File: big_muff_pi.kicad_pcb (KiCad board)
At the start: 2 copper layers, 80 x 100 mm, 67 parts, among them J1 NMJ6HHD2, J2 NMJ6HHD2, J3 Conn_01x05, J4 Conn_01x05, J5 Conn_01x05, J6 Barrel_Jack_MountingPin, Q1 MMBT5551, Q2 MMBT5551, Q3 MMBT5551, Q4 MMBT5551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

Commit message: Estetics finalized.
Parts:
- added D8: floating_green_led, pedale:floating_green_led, F.Cu at (74.0, 117.0)
- added D9: floating_red_led, pedale:floating_red_led, F.Cu at (106.0, 117.0)
- added H5: MountingHole, pedale:M3_hole_with_spacer, F.Cu at (90.0, 145.0)
- added REF**: big_muff_pi_front_plate, pedale:big_muff_pi_front_plate, F.Cu at (90.0, 95.0)
- added RV1: floating_pot_knob, pedale:floating_pot_knob, F.Cu at (68.0, 69.0)
- added RV2: floating_pot_knob, pedale:floating_pot_knob, F.Cu at (90.0, 69.0)
- added RV3: floating_pot_knob, pedale:floating_pot_knob, F.Cu at (112.0, 69.0)
- added RV4: floating_pot, pedale:floating_pot, F.Cu at (68.0, 69.0)
- added RV5: floating_pot, pedale:floating_pot, F.Cu at (90.0, 69.0)
- added RV6: floating_pot, pedale:floating_pot, F.Cu at (112.0, 69.0)
- moved R23 81.4 mm to (56.9, 105.5)
- moved D6 74.0 mm to (59.5, 109.5)
- moved C19 7.18 mm to (60.5, 68.0)
- moved SW1 1.41 mm to (85.0, 122.5)
- moved J2 1.10 mm to (67.2, 133.1)
- moved J1 1.10 mm to (112.8, 116.9)
- moved BT1 0.65 mm to (70.8, 89.7)

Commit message: Est
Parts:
- removed D6: LED, LED_THT:LED_D5.0mm
- removed R23: 1k, Resistor_SMD:R_0603_1608Metric_Pad0.98x0.95mm_HandSolder
- removed REF**: big_muff_pi_front_plate, pedale:big_muff_pi_front_plate
- added P1: big_muff_pi_front_panel, pedale:big_muff_pi_front_plate, F.Cu at (50.0, 50.0)
- added R25: 1k, Resistor_SMD:R_0603_1608Metric_Pad0.98x0.95mm_HandSolder, F.Cu at (61.0, 108.0)
- added R26: 1k, Resistor_SMD:R_0603_1608Metric_Pad0.98x0.95mm_HandSolder, F.Cu at (61.0, 110.5)
- added SIM1: Logo_Open_Hardware_Small, Symbol:OSHW-Logo2_7.3x6mm_SilkScreen, F.Cu at (107.5, 145.0)
- moved D7 70.9 mm to (122.1, 59.6), turned to 180 degrees
- moved C20 66.2 mm to (121.1, 65.9), turned to 180 degrees
- moved C19 55.5 mm to (115.9, 71.9), turned to -90 degrees
- moved R3 48.8 mm to (64.5, 64.1), turned to -90 degrees
- moved C2 46.3 mm to (65.3, 66.7), turned to 0 degrees
- moved R1 45.7 mm to (66.1, 64.1), turned to 90 degrees
- moved R6 43.8 mm to (66.8, 74.6), turned to 90 degrees
- moved J3 43.0 mm to (63.0, 55.0)
- moved J5 43.0 mm to (106.0, 55.0)
- moved R7 39.0 mm to (69.5, 75.4), turned to 0 degrees
- moved R2 38.9 mm to (68.8, 71.1), turned to 90 degrees
- moved R10 38.1 mm to (69.5, 73.7), turned to 0 degrees
- moved R4 38.1 mm to (70.3, 63.4), turned to 0 degrees
- moved C1 37.1 mm to (70.3, 65.0), turned to 0 degrees
- moved Q4 36.3 mm to (70.2, 67.6), turned to 0 degrees
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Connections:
- J3 pad 1: 0 -> 9V
- J3 pad 2: FS_OUT -> Net-(J3-Pin_2)
- J3 pad 4: Net-(J3-Pin_4) -> FS_OUT
- J3 pad 5: 0 -> Net-(J3-Pin_5)
- J5 pad 1: 0 -> Net-(J5-Pin_1)
- J5 pad 5: 0 -> Net-(J5-Pin_5)
- R6 pad 1: Net-(J3-Pin_4) -> Net-(J3-Pin_2)
- SW1 pad 5: Net-(D6-A) -> Net-(J5-Pin_5)
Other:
- board text added: "BIG MUFF PI"

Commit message: Only routing left.
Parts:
- moved R26 75.8 mm to (117.2, 59.7), turned to -90 degrees
- moved C20 67.4 mm to (59.0, 92.1), turned to -90 degrees
- moved D7 67.0 mm to (64.8, 94.4), turned to -90 degrees
- moved C19 59.4 mm to (57.0, 80.0), turned to 90 degrees
- moved R25 55.1 mm to (77.0, 55.3), turned to -90 degrees
- moved R24 48.0 mm to (57.1, 87.7), turned to 90 degrees
- moved C14 44.0 mm to (62.3, 87.0)
- moved Q5 42.3 mm to (60.5, 84.4), turned to 180 degrees
- moved C18 42.1 mm to (62.3, 88.5), turned to 180 degrees
- moved D4 41.0 mm to (64.8, 83.6)
- moved C16 37.5 mm to (63.2, 81.1)
- moved C17 35.5 mm to (63.2, 79.4), turned to 0 degrees
- moved J6 6.30 mm to (63.9, 103.3)
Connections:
- C11 pad 2: Net-(J5-Pin_4) -> Net-(J5-Pin_3)
- C12 pad 2: Net-(J4-Pin_4) -> Net-(J4-Pin_3)
- C13 pad 2: Net-(J4-Pin_2) -> Net-(J4-Pin_1)
- J1 pad S: unconnected-(J1-PadS) -> 0
- J2 pad S: unconnected-(J2-PadS) -> 0
- J3 pad 1: 9V -> Net-(J3-Pin_1)
- J3 pad 3: Net-(J3-Pin_3) -> FS_OUT
- J3 pad 4: FS_OUT -> 9V
- J4 pad 1: 0 -> Net-(J4-Pin_1)
- J4 pad 2: Net-(J4-Pin_2) -> F_OUT
- J4 pad 3: F_OUT -> Net-(J4-Pin_3)
- J4 pad 4: Net-(J4-Pin_4) -> 0
- J5 pad 1: Net-(J5-Pin_1) -> 0
- J5 pad 2: 0 -> Net-(J5-Pin_2)
- R17 pad 2: Net-(J4-Pin_2) -> Net-(J4-Pin_1)
- R22 pad 2: Net-(J4-Pin_4) -> Net-(J4-Pin_3)
- R26 pad 1: Net-(J5-Pin_1) -> Net-(J5-Pin_5)
- R6 pad 1: Net-(J3-Pin_2) -> Net-(J3-Pin_1)
- R7 pad 1: Net-(J3-Pin_3) -> Net-(J3-Pin_2)
- SW1 pad 1: Net-(J5-Pin_3) -> Net-(J5-Pin_2)
- SW1 pad 5: Net-(J5-Pin_5) -> Net-(J5-Pin_4)

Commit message: Lib sync.
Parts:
- SW1: value SW_DPDT_x2 -> pedala_switch; footprint switch:switch_DPDT -> pedale:switch_DPDT
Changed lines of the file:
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@@
 	)
 	(footprint "pedale:floating_red_led"
+		(locked yes)
 		(layer "F.Cu")
 		(at 106 117)
@@
 		)
 	)
-	(footprint "switch:switch_DPDT"
-		(locked yes)
-		(layer "F.Cu")
-		(at 85 122.5)
-		(descr "C&K sub miniature slide switch, JS series, DPDT, right angle, http://www.ckswitches.com/media/1422/js.pdf")
-		(tags "switch DPDT")
-		(property "Reference" "SW1"
-			(at 5 -7 0)
-			(layer "F.SilkS")
-			(hide yes)
-			(effects
-				(font
-					(size 1 1)
-					(thickness 0.15)
-				)
-			)
-		)
-		(property "Value" "SW_DPDT_x2"
-			(at 5 9 0)
-			(layer "F.Fab")
-			(effects
-				(font
-					(size 1 1)
-					(thickness 0.15)
-				)
-			)
-		)
-		(property "Datasheet" ""
-			(at 0 0 0)
-			(unlocked yes)
-			(layer "F.Fab")
-			(hide yes)
-			(effects
-				(font
-					(size 1.27 1.27)
-					(thickness 0.15)
-				)
-			)
-		)
-		(property "Description" "Switch, dual pole double throw, separate symbols"
-			(at 0 0 0)
-			(unlocked yes)
-			(layer "F.Fab")
-			(hide yes)
-			(effects
-				(font
-					(size 1.27 1.27)
-					(thickness 0.15)
-				)
-			)
-		)
-		(property ki_fp_filters "SW*DPDT*")
-		(sheetname "/")
-		(sheetfile "big_muff_pi.kicad_sch")
-		(attr through_hole)
-		(fp_rect
-			(start -5.5 -6)
-			(end 15.5 11)
-			(stroke
-				(width 0.05)
-				(type default)
-			)
-			(fill no)
-			(layer "F.CrtYd")
-		)
-		(fp_text user "${REFERENCE}"
-			(at 6 -7 0)
-			(layer "F.Fab")
-			(effects
-				(font
-					(size 1 1)
-					(thickness 0.15)
-				)
-			)
-		)
-		(pad "1" thru_hole roundrect
-			(at 0 0)
-			(size 3.5 4.5)
-			(drill oval 2.5 3)
-			(layers "*.Cu" "*.Mask")
-			(remove_unused_layers no)
-			(roundrect_rratio 0.2857142857)
-			(net 34 "Net-(J5-Pin_2)")
-			(pinfunction "A")
-			(pintype "passive")
-			(thermal_bridge_angle 45)
-		)
-		(pad "2" thru_hole roundrect
-			(at 5 0)
-			(size 3.5 4.5)
-			(drill oval 2.5 3)
-			(layers "*.Cu" "*.Mask")
-			(remove_unused_layers no)
-			(roundrect_rratio 0.2857142857)
-			(net 35 "Net-(SW1A-B)")
-			(pinfunction "B")
-			(pintype "passive")
-			(thermal_bridge_angle 45)
-		)
-		(pad "3" thru_hole roundrect
-			(at 10 0)
-			(size 3.5 4.5)
-			(drill oval 2.5 3)
-			(layers "*.Cu" "*.Mask")
-			(remove_unused_layers no)
-			(roundrect_rratio 0.2857142857)
-			(net 37 "SW_IN")
-			(pinfunction "C")
-			(pintype "passive")
-			(thermal_bridge_angle 45)
-		)
-		(pad "4" thru_hole roundrect
-			(at 10 5)
-			(size 3.5 4.5)
-			(drill oval 2.5 3)
-			(layers "*.Cu" "*.Mask")
-			(remove_unused_layers no)
-			(roundrect_rratio 0.2857142857)
-			(net 14 "9V")
-			(pinfunction "A")
-			(pintype "passive")
-			(thermal_bridge_angle 45)
-		)
-		(pad "5" thru_hole roundrect
-			(at 5 5)
-			(size 3.5 4.5)
-			(drill oval 2.5 3)
-			(layers "*.Cu" "*.Mask")
-			(remove_unused_layers no)
-			(roundrect_rratio 0.2857142857)
-			(net 32 "Net-(J5-Pin_4)")
-			(pinfunction "B")
-			(pintype "passive")
-			(thermal_bridge_angle 45)
-		)
-		(pad "6" thru_hole roundrect
-			(at 0 5)
-			(size 3.5 4.5)
-			(drill oval 2.5 3)
-			(layers "*.Cu" "*.Mask")
-			(remove_unused_layers no)
-			(roundrect_rratio 0.2857142857)
-			(net 38 "unconnected-(SW1B-C-Pad6)")
-			(pinfunction "C")
-			(pintype "passive+no_connect")
-			(thermal_bridge_angle 45)
-		)
-		(embedded_fonts no)
-		(model "${KIPRJMOD}/switch.STEP"
-			(offset
-				(xyz 5 -2.5 12)
-			)
-			(scale
-				(xyz 1 1 1)
-			)
-			(rotate
-				(xyz -90 -0 -0)
-			)
-		)
-	)
 	(footprint "Diode_SMD:D_SOD-323"
 		(layer "F.Cu")
@@
 		)
 	)
+	(footprint "pedale:switch_DPDT"
+		(locked yes)
+		(layer "F.Cu")
+		(at 85 122.5)
+		(descr "C&K sub miniature slide switch, JS series, DPDT, right angle, http://www.ckswitches.com/media/1422/js.pdf")
+		(tags "switch DPDT")
+		(property "Reference" "SW1"
+			(at 5 -7 0)
+			(layer "F.SilkS")
+			(hide yes)
+			(effects
+				(font
+					(size 1 1)
+					(thickness 0.15)
+				)
+			)
+		)
+		(property "Value" "pedala_switch"
+			(at 5 9 0)
+			(layer "F.Fab")
+			(effects
+				(font
+					(size 1 1)
+					(thickness 0.15)
+				)
+			)
+		)
+		(property "Datasheet" ""
+			(at 0 0 0)
+			(unlocked yes)
+			(layer "F.Fab")
+			(hide yes)
+			(effects
+				(font
+					(size 1.27 1.27)
+					(thickness 0.15)
+				)
+			)
+		)
+		(property "Description" "Switch, dual pole double throw, separate symbols"
+			(at 0 0 0)
+			(unlocked yes)
+			(layer "F.Fab")
+			(hide yes)
+			(effects
+				(font
+					(size 1.27 1.27)
+					(thickness 0.15)
+				)
+			)
+		)
+		(property ki_fp_filters "SW*DPDT*")
+		(sheetname "/")
+		(sheetfile "big_muff_pi.kicad_sch")
+		(attr through_hole)
+		(fp_rect
+			(start -5.5 -6)
+			(end 15.5 11)
+			(stroke
+				(width 0.05)
+				(type default)
+			)
+			(fill no)
+			(layer "F.CrtYd")
+		)
+		(fp_text user "${REFERENCE}"
+			(at 6 -7 0)
+			(layer "F.Fab")
+			(effects
+				(font
+					(size 1 1)
+					(thickness 0.15)
+				)
+			)
+		)
+		(pad "1" thru_hole roundrect
+			(at 0 0)
+			(size 3.5 4.5)
+			(drill oval 2.5 3)
+			(layers "*.Cu" "*.Mask")
+			(remove_unused_layers no)
+			(roundrect_rratio 0.2857142857)
+			(net 34 "Net-(J5-Pin_2)")
+			(pinfunction "A")
+			(pintype "passive")
+			(thermal_bridge_angle 45)
+		)
+		(pad "2" thru_hole roundrect
+			(at 5 0)
+			(size 3.5 4.5)
+			(drill oval 2.5 3)
+			(layers "*.Cu" "*.Mask")
+			(remove_unused_layers no)
+			(roundrect_rratio 0.2857142857)
+			(net 35 "Net-(SW1A-B)")
+			(pinfunction "B")
+			(pintype "passive")
+			(thermal_bridge_angle 45)
+		)
+		(pad "3" thru_hole roundrect
+			(at 10 0)
+			(size 3.5 4.5)
+			(drill oval 2.5 3)
+			(layers "*.Cu" "*.Mask")
+			(remove_unused_layers no)
+			(roundrect_rratio 0.2857142857)
+			(net 37 "SW_IN")
+			(pinfunction "C")
+			(pintype "passive")
+			(thermal_bridge_angle 45)
+		)
+		(pad "4" thru_hole roundrect
+			(at 10 5)
+			(size 3.5 4.5)
+			(drill oval 2.5 3)
+			(layers "*.Cu" "*.Mask")
+			(remove_unused_layers no)
+			(roundrect_rratio 0.2857142857)
+			(net 14 "9V")
+			(pinfunction "A")
+			(pintype "passive")
+			(thermal_bridge_angle 45)
+		)
+		(pad "5" thru_hole roundrect
+			(at 5 5)
+			(size 3.5 4.5)
+			(drill oval 2.5 3)
+			(layers "*.Cu" "*.Mask")
+			(remove_unused_layers no)
+			(roundrect_rratio 0.2857142857)
+			(net 32 "Net-(J5-Pin_4)")
+			(pinfunction "B")
+			(pintype "passive")
+			(thermal_bridge_angle 45)
+		)
+		(pad "6" thru_hole roundrect
+			(at 0 5)
+			(size 3.5 4.5)
+			(drill oval 2.5 3)
+			(layers "*.Cu" "*.Mask")
+			(remove_unused_layers no)
+			(roundrect_rratio 0.2857142857)
+			(net 38 "unconnected-(SW1B-C-Pad6)")
+			(pinfunction "C")
+			(pintype "passive+no_connect")
+			(thermal_bridge_angle 45)
+		)
+		(embedded_fonts no)
+		(model "${KIPRJMOD}/switch.STEP"
+			(offset
+				(xyz 5 -2.5 12)
+			)
+			(scale
+				(xyz 1 1 1)
+			)
+			(rotate
+				(xyz -90 -0 -0)
+			)
+		)
+	)
 	(footprint "Package_TO_SOT_SMD:SOT-23"
 		(layer "F.Cu")
@@
 	)
 	(footprint "pedale:floating_green_led"
+		(locked yes)
 		(layer "F.Cu")
 		(at 74 117)
@@
 			(unlocked yes)
 			(layer "F.SilkS")
+			(hide yes)
 			(effects
 				(font

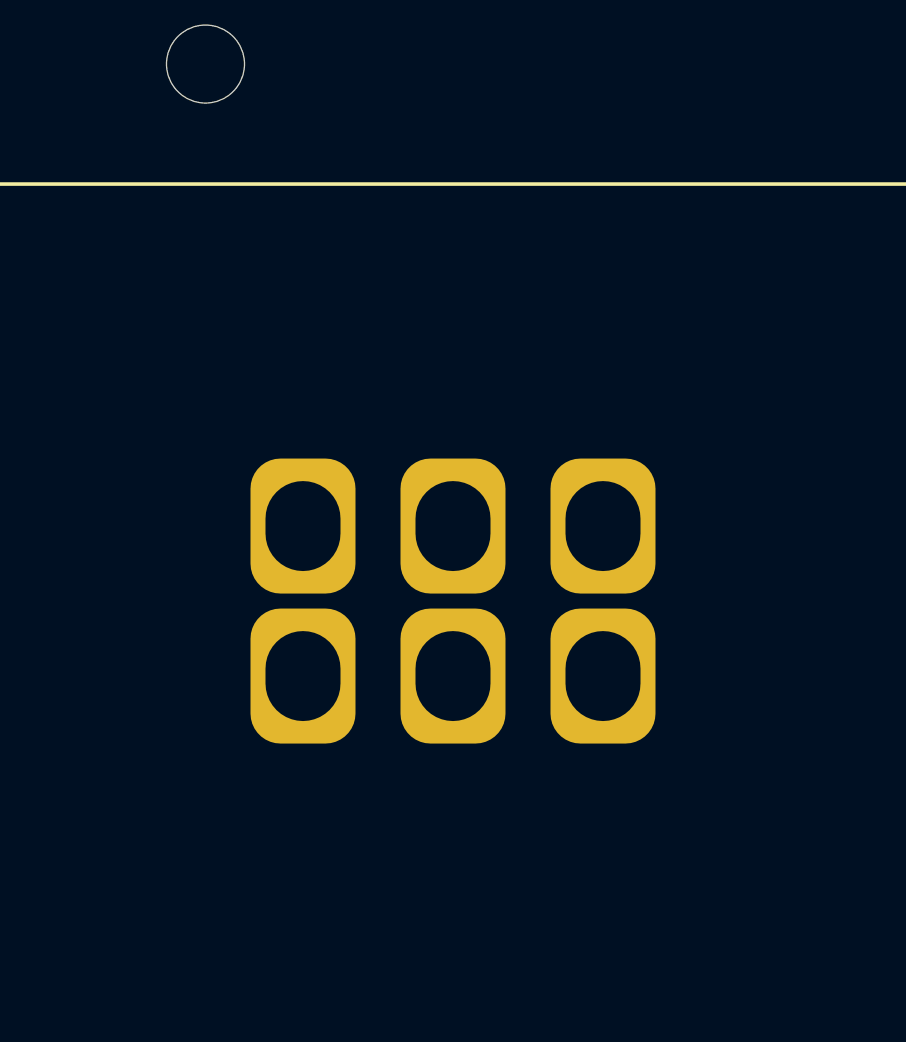
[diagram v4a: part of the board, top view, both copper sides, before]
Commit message: New switch
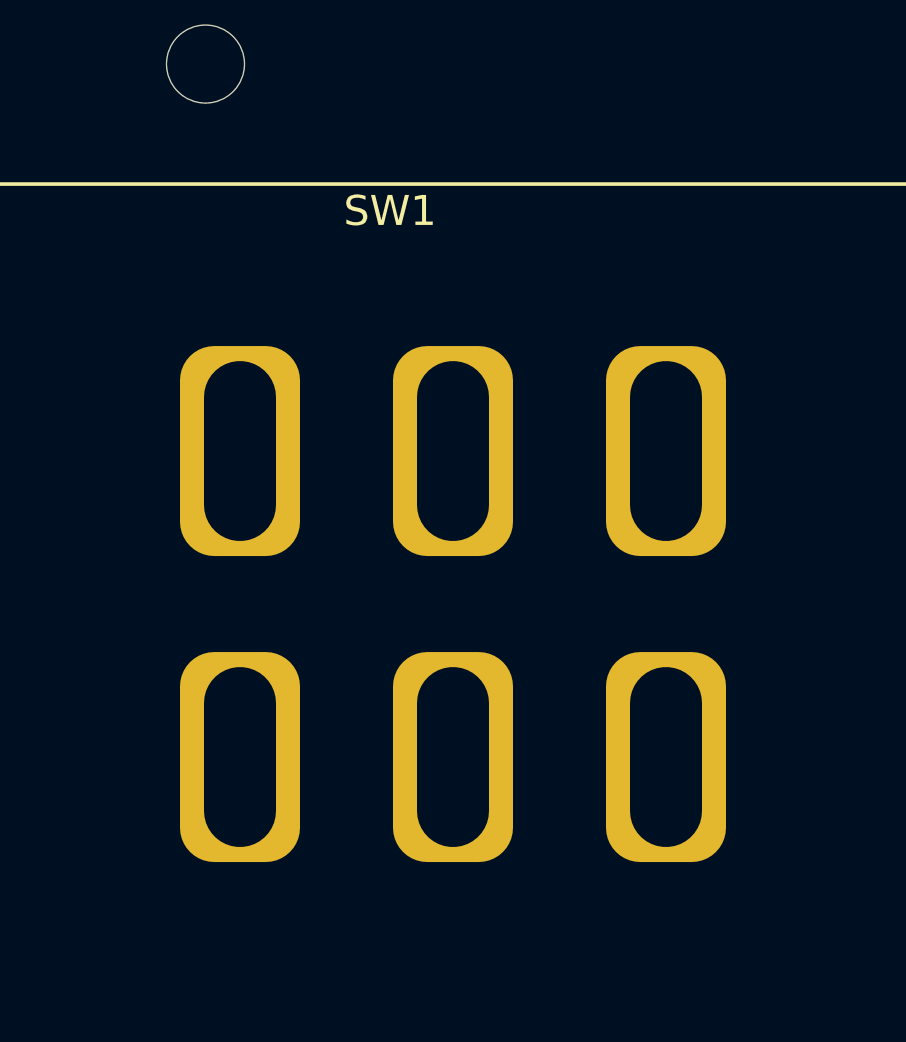
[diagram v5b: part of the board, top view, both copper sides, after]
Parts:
- SW1: footprint pedale:switch_DPDT -> pedale:foot_switch
- moved SW1 4.08 mm to (82.9, 119.0)
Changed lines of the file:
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@@
 		)
 	)
+	(footprint "pedale:foot_switch"
+		(layer "F.Cu")
+		(at 82.9 119)
+		(descr "C&K sub miniature slide switch, JS series, DPDT, right angle, http://www.ckswitches.com/media/1422/js.pdf")
+		(tags "switch DPDT")
+		(property "Reference" "SW1"
+			(at 5 -7 0)
+			(layer "F.SilkS")
+			(effects
+				(font
+					(size 1 1)
+					(thickness 0.15)
+				)
+			)
+		)
+		(property "Value" "pedala_switch"
+			(at 5 9 0)
+			(layer "F.Fab")
+			(effects
+				(font
+					(size 1 1)
+					(thickness 0.15)
+				)
+			)
+		)
+		(property "Datasheet" ""
+			(at 0 0 0)
+			(unlocked yes)
+			(layer "F.Fab")
+			(hide yes)
+			(effects
+				(font
+					(size 1.27 1.27)
+					(thickness 0.15)
+				)
+			)
+		)
+		(property "Description" "Switch, dual pole double throw, separate symbols"
+			(at 0 0 0)
+			(unlocked yes)
+			(layer "F.Fab")
+			(hide yes)
+			(effects
+				(font
+					(size 1.27 1.27)
+					(thickness 0.15)
+				)
+			)
+		)
+		(property ki_fp_filters "SW*DPDT*")
+		(sheetname "/")
+		(sheetfile "big_muff_pi.kicad_sch")
+		(attr through_hole)
+		(fp_rect
+			(start -3.5 -3)
+			(end 18 15)
+			(stroke
+				(width 0.05)
+				(type default)
+			)
+			(fill no)
+			(layer "F.CrtYd")
+		)
+		(fp_text user "${REFERENCE}"
+			(at 6 -7 0)
+			(layer "F.Fab")
+			(effects
+				(font
+					(size 1 1)
+					(thickness 0.15)
+				)
+			)
+		)
+		(pad "1" thru_hole roundrect
+			(at 0 1)
+			(size 4 7)
+			(drill oval 2.4 6)
+			(layers "*.Cu" "*.Mask")
+			(remove_unused_layers no)
+			(roundrect_rratio 0.2857142857)
+			(net 34 "Net-(J5-Pin_2)")
+			(pinfunction "A")
+			(pintype "passive")
+			(thermal_bridge_angle 45)
+		)
+		(pad "2" thru_hole roundrect
+			(at 7.1 1)
+			(size 4 7)
+			(drill oval 2.4 6)
+			(layers "*.Cu" "*.Mask")
+			(remove_unused_layers no)
+			(roundrect_rratio 0.2857142857)
+			(net 35 "Net-(SW1A-B)")
+			(pinfunction "B")
+			(pintype "passive")
+			(thermal_bridge_angle 45)
+		)
+		(pad "3" thru_hole roundrect
+			(at 14.2 1)
+			(size 4 7)
+			(drill oval 2.4 6)
+			(layers "*.Cu" "*.Mask")
+			(remove_unused_layers no)
+			(roundrect_rratio 0.2857142857)
+			(net 37 "SW_IN")
+			(pinfunction "C")
+			(pintype "passive")
+			(thermal_bridge_angle 45)
+		)
+		(pad "4" thru_hole roundrect
+			(at 14.2 11.2)
+			(size 4 7)
+			(drill oval 2.4 6)
+			(layers "*.Cu" "*.Mask")
+			(remove_unused_layers no)
+			(roundrect_rratio 0.2857142857)
+			(net 14 "9V")
+			(pinfunction "A")
+			(pintype "passive")
+			(thermal_bridge_angle 45)
+		)
+		(pad "5" thru_hole roundrect
+			(at 7.1 11.2)
+			(size 4 7)
+			(drill oval 2.4 6)
+			(layers "*.Cu" "*.Mask")
+			(remove_unused_layers no)
+			(roundrect_rratio 0.2857142857)
+			(net 32 "Net-(J5-Pin_4)")
+			(pinfunction "B")
+			(pintype "passive")
+			(thermal_bridge_angle 45)
+		)
+		(pad "6" thru_hole roundrect
+			(at 0 11.2)
+			(size 4 7)
+			(drill oval 2.4 6)
+			(layers "*.Cu" "*.Mask")
+			(remove_unused_layers no)
+			(roundrect_rratio 0.2857142857)
+			(net 38 "unconnected-(SW1B-C-Pad6)")
+			(pinfunction "C")
+			(pintype "passive+no_connect")
+			(thermal_bridge_angle 45)
+		)
+		(embedded_fonts no)
+		(model "${KIPRJMOD}/pedale.pretty/dpdt_pci.stp"
+			(offset
+				(xyz 7 -6 0)
+			)
+			(scale
+				(xyz 1 1 1)
+			)
+			(rotate
+				(xyz -90 -0 -90)
+			)
+		)
+	)
 	(footprint "Connector_BarrelJack:BarrelJack_GCT_DCJ200-10-A_Horizontal"
 		(locked yes)
@@
 			)
 		)
-	)
-	(footprint "pedale:switch_DPDT"
-		(locked yes)
-		(layer "F.Cu")
-		(at 85 122.5)
-		(descr "C&K sub miniature slide switch, JS series, DPDT, right angle, http://www.ckswitches.com/media/1422/js.pdf")
-		(tags "switch DPDT")
-		(property "Reference" "SW1"
-			(at 5 -7 0)
-			(layer "F.SilkS")
-			(hide yes)
-			(effects
-				(font
-					(size 1 1)
-					(thickness 0.15)
-				)
-			)
-		)
-		(property "Value" "pedala_switch"
-			(at 5 9 0)
-			(layer "F.Fab")
-			(effects
-				(font
-					(size 1 1)
-					(thickness 0.15)
-				)
-			)
-		)
-		(property "Datasheet" ""
-			(at 0 0 0)
-			(unlocked yes)
-			(layer "F.Fab")
-			(hide yes)
-			(effects
-				(font
-					(size 1.27 1.27)
-					(thickness 0.15)
-				)
-			)
-		)
-		(property "Description" "Switch, dual pole double throw, separate symbols"
-			(at 0 0 0)
-			(unlocked yes)
-			(layer "F.Fab")
-			(hide yes)
-			(effects
-				(font
-					(size 1.27 1.27)
-					(thickness 0.15)
-				)
-			)
-		)
-		(property ki_fp_filters "SW*DPDT*")
-		(sheetname "/")
-		(sheetfile "big_muff_pi.kicad_sch")
-		(attr through_hole)
-		(fp_rect
-			(start -5.5 -6)
-			(end 15.5 11)
-			(stroke
-				(width 0.05)
-				(type default)
-			)
-			(fill no)
-			(layer "F.CrtYd")
-		)
-		(fp_text user "${REFERENCE}"
-			(at 6 -7 0)
-			(layer "F.Fab")
-			(effects
-				(font
-					(size 1 1)
-					(thickness 0.15)
-				)
-			)
-		)
-		(pad "1" thru_hole roundrect
-			(at 0 0)
-			(size 3.5 4.5)
-			(drill oval 2.5 3)
-			(layers "*.Cu" "*.Mask")
-			(remove_unused_layers no)
-			(roundrect_rratio 0.2857142857)
-			(net 34 "Net-(J5-Pin_2)")
-			(pinfunction "A")
-			(pintype "passive")
-			(thermal_bridge_angle 45)
-		)
-		(pad "2" thru_hole roundrect
-			(at 5 0)
-			(size 3.5 4.5)
-			(drill oval 2.5 3)
-			(layers "*.Cu" "*.Mask")
-			(remove_unused_layers no)
-			(roundrect_rratio 0.2857142857)
-			(net 35 "Net-(SW1A-B)")
-			(pinfunction "B")
-			(pintype "passive")
-			(thermal_bridge_angle 45)
-		)
-		(pad "3" thru_hole roundrect
-			(at 10 0)
-			(size 3.5 4.5)
-			(drill oval 2.5 3)
-			(layers "*.Cu" "*.Mask")
-			(remove_unused_layers no)
-			(roundrect_rratio 0.2857142857)
-			(net 37 "SW_IN")
-			(pinfunction "C")
-			(pintype "passive")
-			(thermal_bridge_angle 45)
-		)
-		(pad "4" thru_hole roundrect
-			(at 10 5)
-			(size 3.5 4.5)
-			(drill oval 2.5 3)
-			(layers "*.Cu" "*.Mask")
-			(remove_unused_layers no)
-			(roundrect_rratio 0.2857142857)
-			(net 14 "9V")
-			(pinfunction "A")
-			(pintype "passive")
-			(thermal_bridge_angle 45)
-		)
-		(pad "5" thru_hole roundrect
-			(at 5 5)
-			(size 3.5 4.5)
-			(drill oval 2.5 3)
-			(layers "*.Cu" "*.Mask")
-			(remove_unused_layers no)
-			(roundrect_rratio 0.2857142857)
-			(net 32 "Net-(J5-Pin_4)")
-			(pinfunction "B")
-			(pintype "passive")
-			(thermal_bridge_angle 45)
-		)
-		(pad "6" thru_hole roundrect
-			(at 0 5)
-			(size 3.5 4.5)
-			(drill oval 2.5 3)
-			(layers "*.Cu" "*.Mask")
-			(remove_unused_layers no)
-			(roundrect_rratio 0.2857142857)
-			(net 38 "unconnected-(SW1B-C-Pad6)")
-			(pinfunction "C")
-			(pintype "passive+no_connect")
-			(thermal_bridge_angle 45)
-		)
-		(embedded_fonts no)
-		(model "${KIPRJMOD}/switch.STEP"
-			(offset
-				(xyz 5 -2.5 12)
-			)
-			(scale
-				(xyz 1 1 1)
-			)
-			(rotate
-				(xyz -90 -0 -0)
-			)
-		)
